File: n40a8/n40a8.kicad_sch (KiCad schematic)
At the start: 92 parts, among them SW1 CPG151101S11-16, SW10 CPG151101S11-16, SW11 CPG151101S11-16, SW12 CPG151101S11-16, SW13 CPG151101S11-16, SW14 CPG151101S11-16, SW15 CPG151101S11-16, SW16 CPG151101S11-16, SW17 CPG151101S11-16, SW18 CPG151101S11-16, SW19 CPG151101S11-16, SW2 CPG151101S11-16, SW20 CPG151101S11-16, SW21 CPG151101S11-16, SW22 CPG151101S11-16, SW23 CPG151101S11-16, SW24 CPG151101S11-16, SW25 CPG151101S11-16, SW26 CPG151101S11-16, SW27 CPG151101S11-16, SW28 CPG151101S11-16, SW29 CPG151101S11-16, SW3 CPG151101S11-16, SW30 CPG151101S11-16, SW31 CPG151101S11-16, SW32 CPG151101S11-16, SW33 CPG151101S11-16, SW34 CPG151101S11-16, SW35 CPG151101S11-16, SW36 CPG151101S11-16, SW37 CPG151101S11-16, SW38 CPG151101S11-16, SW39 CPG151101S11-16, SW4 CPG151101S11-16, SW40 CPG151101S11-16, SW41 CPG151101S11-16, SW42 CPG151101S11-16, SW43 SW_RST, SW44 SW_PWR, SW5 CPG151101S11-16, SW6 CPG151101S11-16, SW7 CPG151101S11-16, SW8 CPG151101S11-16, SW9 CPG151101S11-16, U1 BLE-Micro-Pro-2, U2 TPS61221

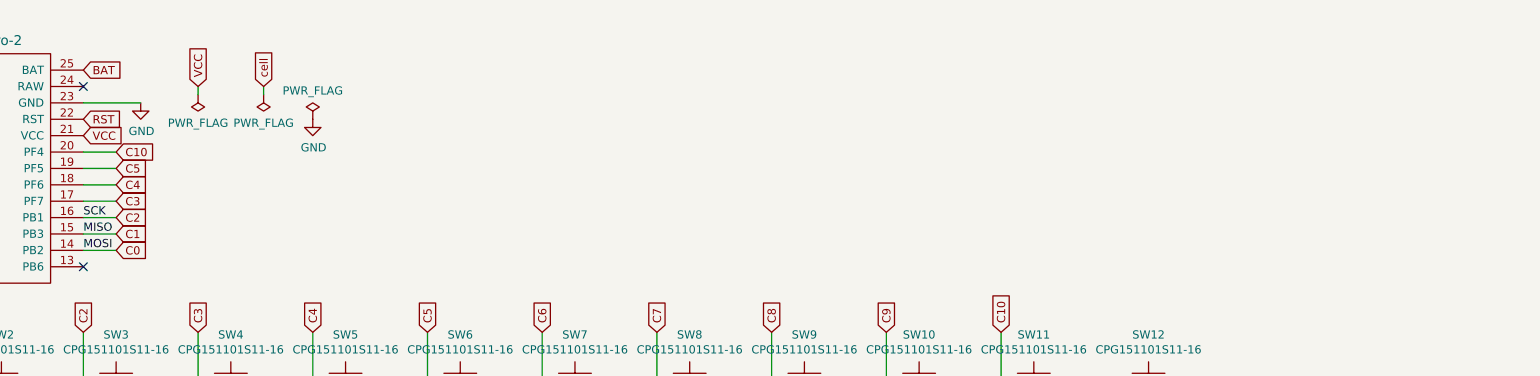
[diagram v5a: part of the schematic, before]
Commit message: modified wiring
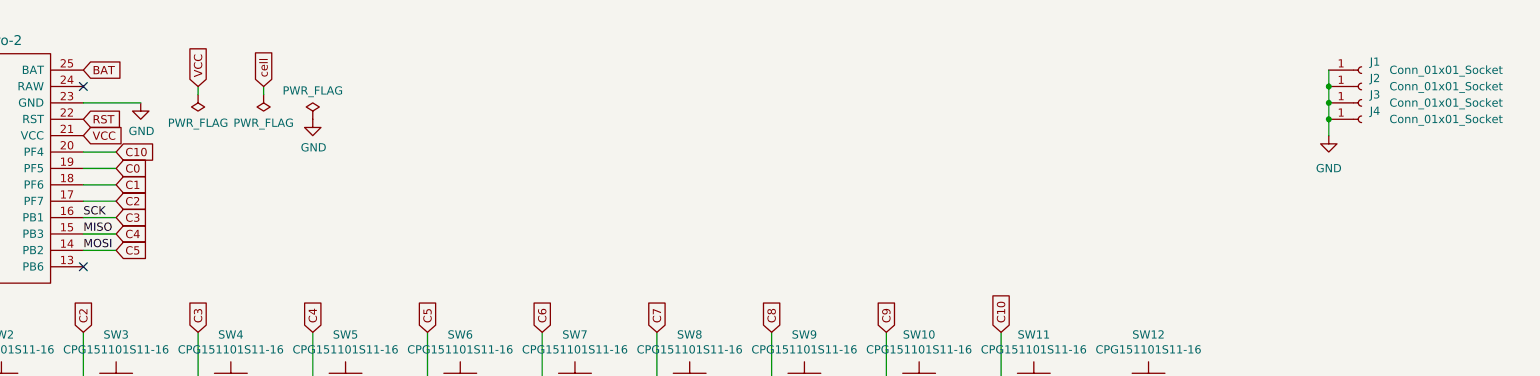
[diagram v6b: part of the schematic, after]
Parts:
- added J1, J2, J3, J4: Conn_01x01_Socket, cscslib:HOLE_M2, symbol Connector:Conn_01x01_Socket
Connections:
- net C0: now also U1.19 (PF5); no longer U1.14 (PB2)
- net C1: now also U1.18 (PF6); no longer U1.15 (PB3)
- net C2: now also U1.17 (PF7); no longer U1.16 (PB1)
- net C3: now also U1.16 (PB1); no longer U1.17 (PF7)
- net C4: now also U1.15 (PB3); no longer U1.18 (PF6)
- net C5: now also U1.14 (PB2); no longer U1.19 (PF5)
- net GND: now also J1.1 (Pin_1), J2.1 (Pin_1), J3.1 (Pin_1), J4.1 (Pin_1)
